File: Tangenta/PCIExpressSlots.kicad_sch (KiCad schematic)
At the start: 2 parts, among them J3 10018784-10213TLF, J4 10018784-10213TLF

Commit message: ...
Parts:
- added J10: 1-2199230-5, M2_Slot:M2_Slot, symbol M2_Slot:1-2199230-5
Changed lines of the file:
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@@
+    )
+  )
+  (symbol (lib_id "M2_Slot:1-2199230-5") (at 259.08 67.31 90) (mirror x) (unit 1)
+    (in_bom yes) (on_board yes) (dnp no)
+    (property "Reference" "J10" (at 251.46 69.85 90)
+      (effects (font (size 1.27 1.27)) (justify right))
+    )
+    (property "Value" "1-2199230-5" (at 252.73 170.815 90)
+      (effects (font (size 1.27 1.27)) (justify right))
+    )
+    (property "Footprint" "M2_Slot:M2_Slot" (at 348.92 162.56 0)
+      (effects (font (size 1.27 1.27)) (justify left top) hide)
+    )
+    (property "Datasheet" "https://www.te.com/commerce/DocumentDelivery/DDEController?Action=srchrtrv&DocNm=1-1773702-1NGFFQRG-EN&DocType=Data+Sheet&DocLang=English&PartCntxt=1-2199230-5&DocFormat=pdf" (at 448.92 162.56 0)
+      (effects (font (size 1.27 1.27)) (justify left top) hide)
+    )
+    (property "Height" "4.2" (at 648.92 162.56 0)
+      (effects (font (size 1.27 1.27)) (justify left top) hide)
+    )
+    (property "Manufacturer_Name" "TE Connectivity" (at 748.92 162.56 0)
+      (effects (font (size 1.27 1.27)) (justify left top) hide)
+    )
+    (property "Manufacturer_Part_Number" "1-2199230-5" (at 848.92 162.56 0)
+      (effects (font (size 1.27 1.27)) (justify left top) hide)
+    )
+    (property "Mouser Part Number" "571-1-2199230-5" (at 948.92 162.56 0)
+      (effects (font (size 1.27 1.27)) (justify left top) hide)
+    )
+    (property "Mouser Price/Stock" "https://www.mouser.co.uk/ProductDetail/TE-Connectivity/1-2199230-5?qs=N0TJGnUfxCD5L9UvFjPEwQ%3D%3D" (at 1048.92 162.56 0)
+      (effects (font (size 1.27 1.27)) (justify left top) hide)
+    )
+    (property "Arrow Part Number" "1-2199230-5" (at 1148.92 162.56 0)
+      (effects (font (size 1.27 1.27)) (justify left top) hide)
+    )
+    (property "Arrow Price/Stock" "https://www.arrow.com/en/products/1-2199230-5/te-connectivity?region=nac" (at 1248.92 162.56 0)
+      (effects (font (size 1.27 1.27)) (justify left top) hide)
+    )
+    (pin "1")
+    (pin "10")
+    (pin "11")
+    (pin "12")
+    (pin "13")
+    (pin "14")
+    (pin "15")
+    (pin "16")
+    (pin "17")
+    (pin "18")
+    (pin "19")
+    (pin "2")
+    (pin "20")
+    (pin "21")
+    (pin "22")
+    (pin "23")
+    (pin "24")
+    (pin "25")
+    (pin "26")
+    (pin "27")
+    (pin "28")
+    (pin "29")
+    (pin "3")
+    (pin "30")
+    (pin "31")
+    (pin "32")
+    (pin "33")
+    (pin "34")
+    (pin "35")
+    (pin "36")
+    (pin "37")
+    (pin "38")
+    (pin "39")
+    (pin "4")
+    (pin "40")
+    (pin "41")
+    (pin "42")
+    (pin "43")
+    (pin "44")
+    (pin "45")
+    (pin "46")
+    (pin "47")
+    (pin "48")
+    (pin "49")
+    (pin "5")
+    (pin "50")
+    (pin "51")
+    (pin "52")
+    (pin "53")
+    (pin "54")
+    (pin "55")
+    (pin "56")
+    (pin "57")
+    (pin "58")
+    (pin "6")
+    (pin "67")
+    (pin "68")
+    (pin "69")
+    (pin "7")
+    (pin "70")
+    (pin "71")
+    (pin "72")
+    (pin "73")
+    (pin "74")
+    (pin "75")
+    (pin "8")
+    (pin "9")
+    (pin "MP1")
+    (pin "MP2")
+    (instances
+      (project "Tangenta"
+        (path "/358d1bcf-7599-4352-8c4d-baa18a5f09e6/9b1f6f94-444c-4c59-8de9-290bde336856"
+          (reference "J10") (unit 1)
+        )
+      )
     )
   )

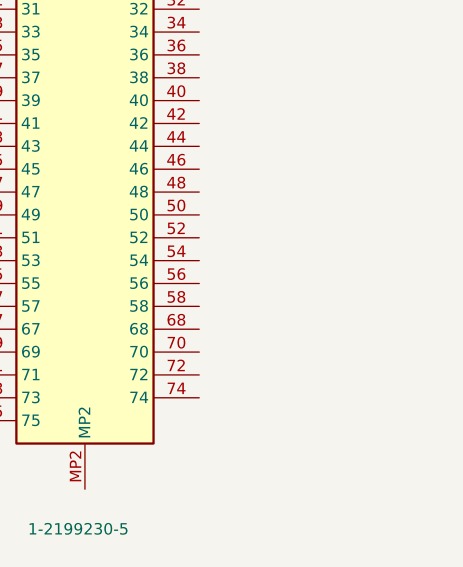
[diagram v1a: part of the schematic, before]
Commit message: Standoffs revisited.
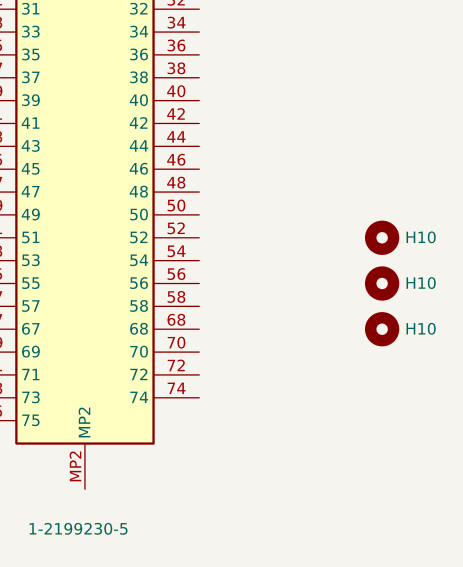
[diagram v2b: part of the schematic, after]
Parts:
- added H10 (x3): MountingHole, MountingHole:MountingHole_2.2mm_M2_Pad, symbol Mechanical:MountingHole
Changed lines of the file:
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@@
 (kicad_sch (version 20230121) (generator eeschema)
   (paper "A3")
+  (symbol (lib_id "Mechanical:MountingHole") (at 292.1 148.59 0) (unit 1)
+    (in_bom yes) (on_board yes) (dnp no)
+    (property "Reference" "H10" (at 294.64 148.59 0)
+      (effects (font (size 1.27 1.27)) (justify left))
+    )
+    (property "Value" "MountingHole" (at 294.64 149.86 0)
+      (effects (font (size 1.27 1.27)) (justify left) hide)
+    )
+    (property "Footprint" "MountingHole:MountingHole_2.2mm_M2_Pad" (at 292.1 148.59 0)
+      (effects (font (size 1.27 1.27)) hide)
+    )
+    (property "Datasheet" "~" (at 292.1 148.59 0)
+      (effects (font (size 1.27 1.27)) hide)
+    )
+    (instances
+      (project "Tangenta"
+        (path "/358d1bcf-7599-4352-8c4d-baa18a5f09e6/f1c5822c-e7b8-40ae-bab0-71fd1c2cfc7c"
+          (reference "H10") (unit 1)
+        )
+        (path "/358d1bcf-7599-4352-8c4d-baa18a5f09e6/9b1f6f94-444c-4c59-8de9-290bde336856"
+          (reference "H14") (unit 1)
+        )
+      )
+    )
+  )
   (symbol (lib_id "PCIE_x16_Slot:10018784-10213TLF") (at 69.85 44.45 0) (unit 1)
     (in_bom yes) (on_board yes) (dnp no) (fields_autoplaced)
@@
         )
       )
+    )
+  )
+  (symbol (lib_id "Mechanical:MountingHole") (at 292.1 143.51 0) (unit 1)
+    (in_bom yes) (on_board yes) (dnp no)
+    (property "Reference" "H10" (at 294.64 143.51 0)
+      (effects (font (size 1.27 1.27)) (justify left))
+    )
+    (property "Value" "MountingHole" (at 294.64 144.78 0)
+      (effects (font (size 1.27 1.27)) (justify left) hide)
+    )
+    (property "Footprint" "MountingHole:MountingHole_2.2mm_M2_Pad" (at 292.1 143.51 0)
+      (effects (font (size 1.27 1.27)) hide)
+    )
+    (property "Datasheet" "~" (at 292.1 143.51 0)
+      (effects (font (size 1.27 1.27)) hide)
+    )
+    (instances
+      (project "Tangenta"
+        (path "/358d1bcf-7599-4352-8c4d-baa18a5f09e6/f1c5822c-e7b8-40ae-bab0-71fd1c2cfc7c"
+          (reference "H10") (unit 1)
+        )
+        (path "/358d1bcf-7599-4352-8c4d-baa18a5f09e6/9b1f6f94-444c-4c59-8de9-290bde336856"
+          (reference "H13") (unit 1)
+        )
+      )
+    )
+  )
+  (symbol (lib_id "Mechanical:MountingHole") (at 292.1 138.43 0) (unit 1)
+    (in_bom yes) (on_board yes) (dnp no)
+    (property "Reference" "H10" (at 294.64 138.43 0)
+      (effects (font (size 1.27 1.27)) (justify left))
+    )
+    (property "Value" "MountingHole" (at 294.64 139.7 0)
+      (effects (font (size 1.27 1.27)) (justify left) hide)
+    )
+    (property "Footprint" "MountingHole:MountingHole_2.2mm_M2_Pad" (at 292.1 138.43 0)
+      (effects (font (size 1.27 1.27)) hide)
+    )
+    (property "Datasheet" "~" (at 292.1 138.43 0)
+      (effects (font (size 1.27 1.27)) hide)
+    )
+    (instances
+      (project "Tangenta"
+        (path "/358d1bcf-7599-4352-8c4d-baa18a5f09e6/f1c5822c-e7b8-40ae-bab0-71fd1c2cfc7c"
+          (reference "H10") (unit 1)
+        )
+        (path "/358d1bcf-7599-4352-8c4d-baa18a5f09e6/9b1f6f94-444c-4c59-8de9-290bde336856"
+          (reference "H12") (unit 1)
+        )
+      )
